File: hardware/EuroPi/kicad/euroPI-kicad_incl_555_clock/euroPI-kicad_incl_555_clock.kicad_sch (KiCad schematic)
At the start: 119 parts, among them J1 Output 1 Jack, J10 Eurorack Power 2x8 16p, J11 Conn_01x13_Socket, J12 OLED 64x128, J13 USB_B_Micro, J14 Conn_01x03_Pin, J15 Conn_01x04_Pin, J16 Conn_02x04_Top_Bottom, J17 Conn_01x13_Pin, J18 Conn_01x04_Pin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

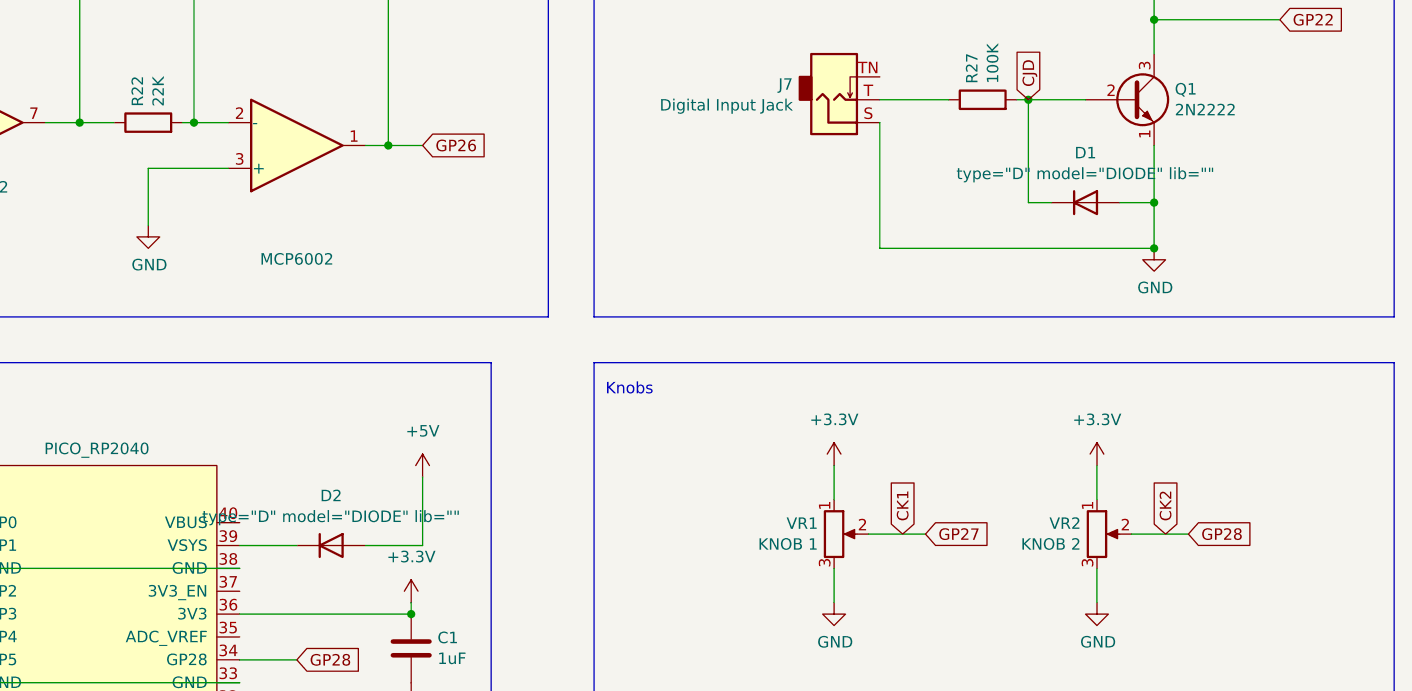
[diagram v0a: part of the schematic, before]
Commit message: wip tried a reroute should move power rail caps closer i think
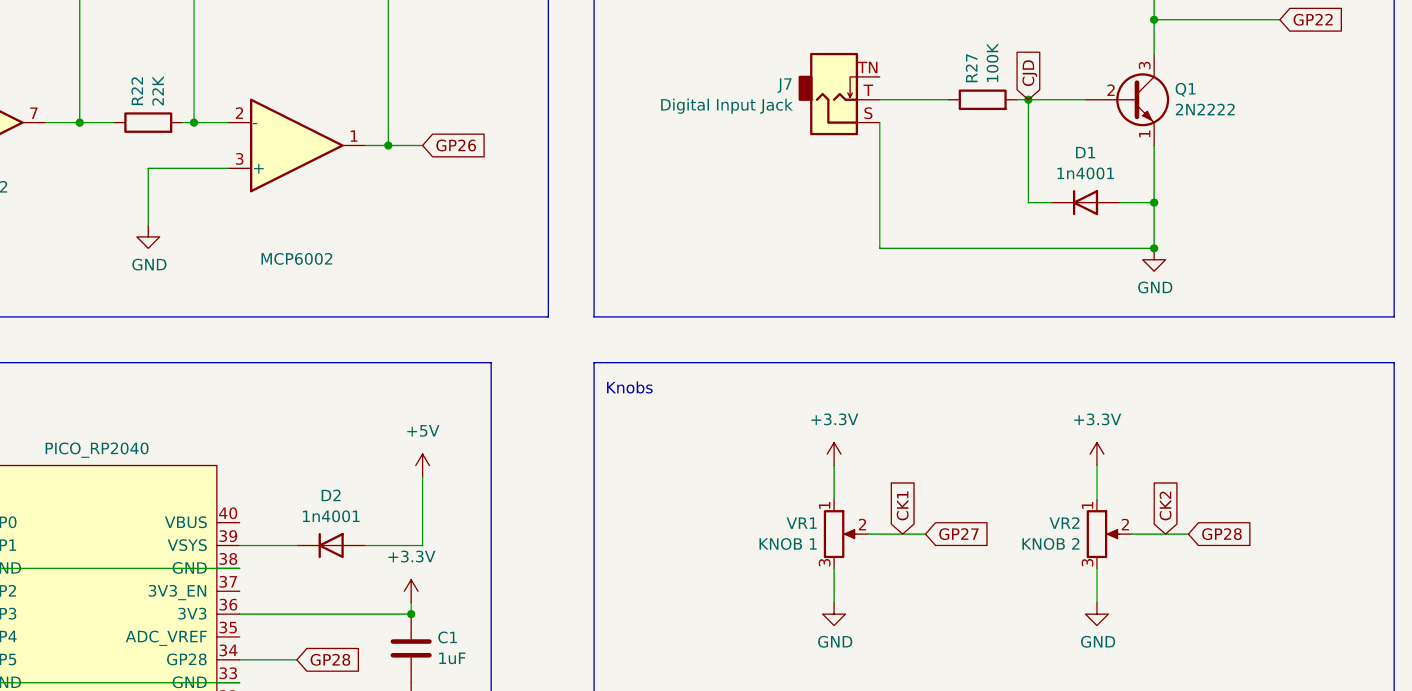
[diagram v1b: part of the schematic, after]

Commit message: reorg continued mainly trying to get power filtering better situated
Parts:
- O, O? (x8): footprint Package_DIP:DIP-14_W7.62mm_Socket -> Library:DIP-14_W7.62mm_Socket_gap_in_the_middle
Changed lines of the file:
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@@
       (effects (font (size 1.27 1.27)))
     )
-    (property "Footprint" "Package_DIP:DIP-14_W7.62mm_Socket" (at 342.9 35.56 0)
+    (property "Footprint" "Library:DIP-14_W7.62mm_Socket_gap_in_the_middle" (at 342.9 35.56 0)
       (effects (font (size 1.27 1.27)) hide)
     )
@@
       (effects (font (size 1.27 1.27)))
     )
-    (property "Footprint" "Package_DIP:DIP-14_W7.62mm_Socket" (at 153.67 35.56 0)
+    (property "Footprint" "Library:DIP-14_W7.62mm_Socket_gap_in_the_middle" (at 153.67 35.56 0)
       (effects (font (size 1.27 1.27)) hide)
     )
@@
       (effects (font (size 1.27 1.27)))
     )
-    (property "Footprint" "Package_DIP:DIP-14_W7.62mm_Socket" (at 247.65 35.56 0)
+    (property "Footprint" "Library:DIP-14_W7.62mm_Socket_gap_in_the_middle" (at 247.65 35.56 0)
       (effects (font (size 1.27 1.27)) hide)
     )
@@
       (effects (font (size 1.27 1.27)))
     )
-    (property "Footprint" "Package_DIP:DIP-14_W7.62mm_Socket" (at 342.9 91.44 0)
+    (property "Footprint" "Library:DIP-14_W7.62mm_Socket_gap_in_the_middle" (at 342.9 91.44 0)
       (effects (font (size 1.27 1.27)) hide)
     )
@@
       (effects (font (size 1.27 1.27)))
     )
-    (property "Footprint" "Package_DIP:DIP-14_W7.62mm_Socket" (at 153.67 91.44 0)
+    (property "Footprint" "Library:DIP-14_W7.62mm_Socket_gap_in_the_middle" (at 153.67 91.44 0)
       (effects (font (size 1.27 1.27)) hide)
     )
@@
       (effects (font (size 1.27 1.27)))
     )
-    (property "Footprint" "Package_DIP:DIP-14_W7.62mm_Socket" (at 247.65 91.44 0)
+    (property "Footprint" "Library:DIP-14_W7.62mm_Socket_gap_in_the_middle" (at 247.65 91.44 0)
       (effects (font (size 1.27 1.27)) hide)
     )
@@
       (effects (font (size 1.27 1.27)))
     )
-    (property "Footprint" "Package_DIP:DIP-14_W7.62mm_Socket" (at 240.03 180.34 0)
+    (property "Footprint" "Library:DIP-14_W7.62mm_Socket_gap_in_the_middle" (at 240.03 180.34 0)
       (effects (font (size 1.27 1.27)) hide)
     )
@@
       (effects (font (size 1.27 1.27)))
     )
-    (property "Footprint" "Package_DIP:DIP-14_W7.62mm_Socket" (at 146.05 231.14 0)
+    (property "Footprint" "Library:DIP-14_W7.62mm_Socket_gap_in_the_middle" (at 146.05 231.14 0)
       (effects (font (size 1.27 1.27)) hide)
     )
@@
       (effects (font (size 1.27 1.27)))
     )
-    (property "Footprint" "Package_DIP:DIP-14_W7.62mm_Socket" (at 166.37 231.14 0)
+    (property "Footprint" "Library:DIP-14_W7.62mm_Socket_gap_in_the_middle" (at 166.37 231.14 0)
       (effects (font (size 1.27 1.27)) hide)
     )

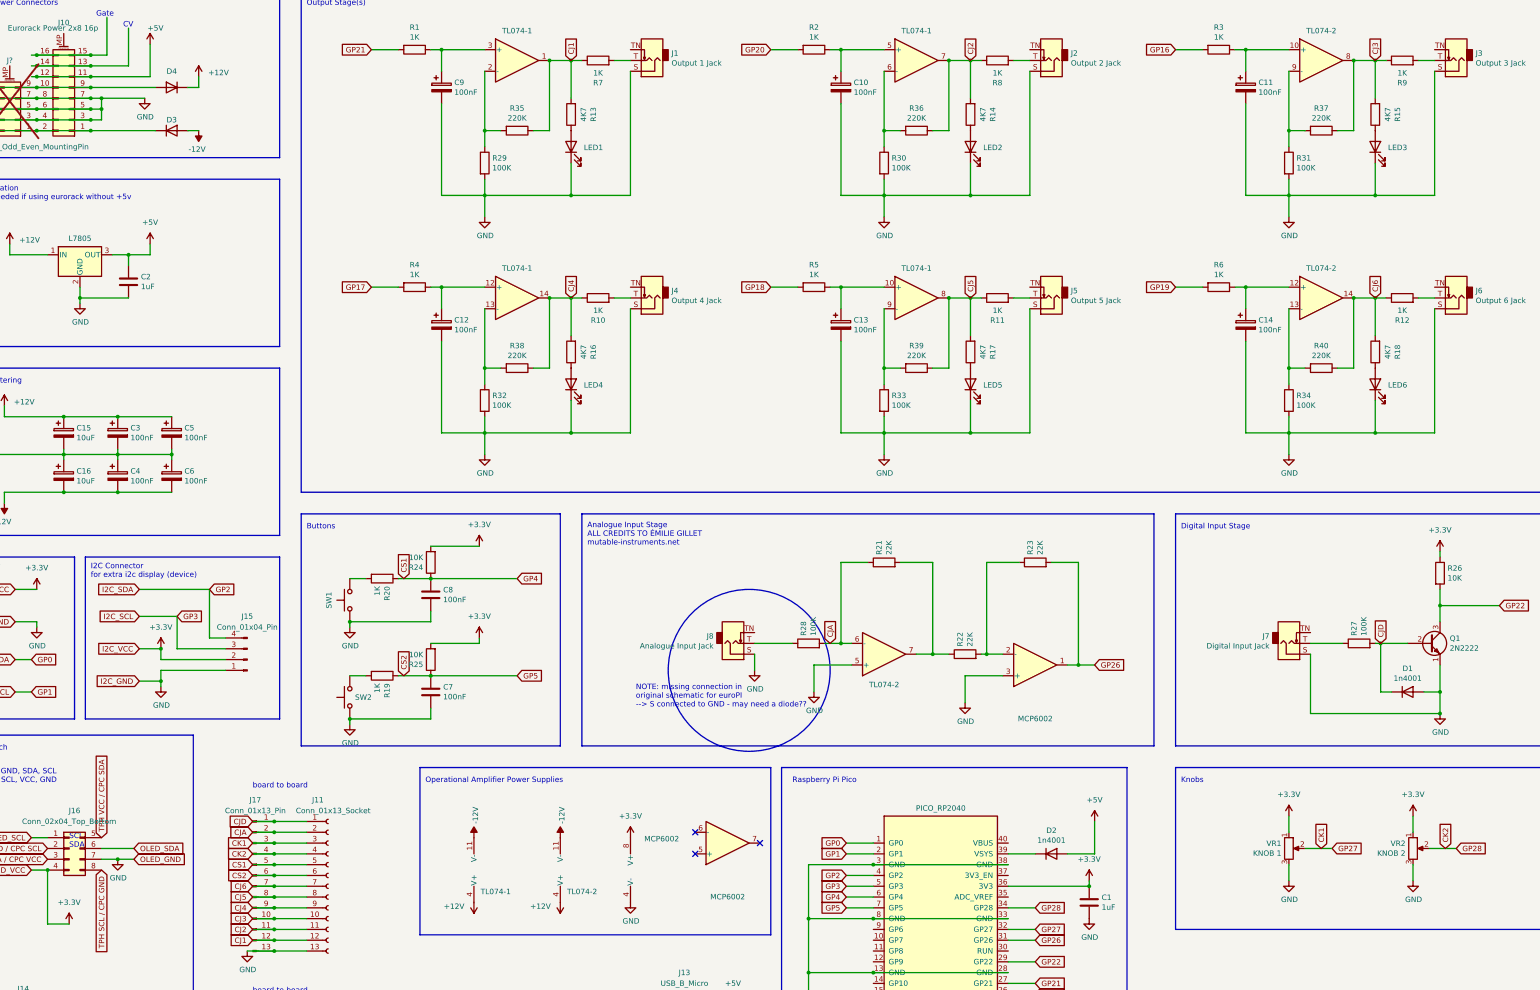
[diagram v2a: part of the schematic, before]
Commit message: updated with caps under sockets in order to improve power filtering as intended
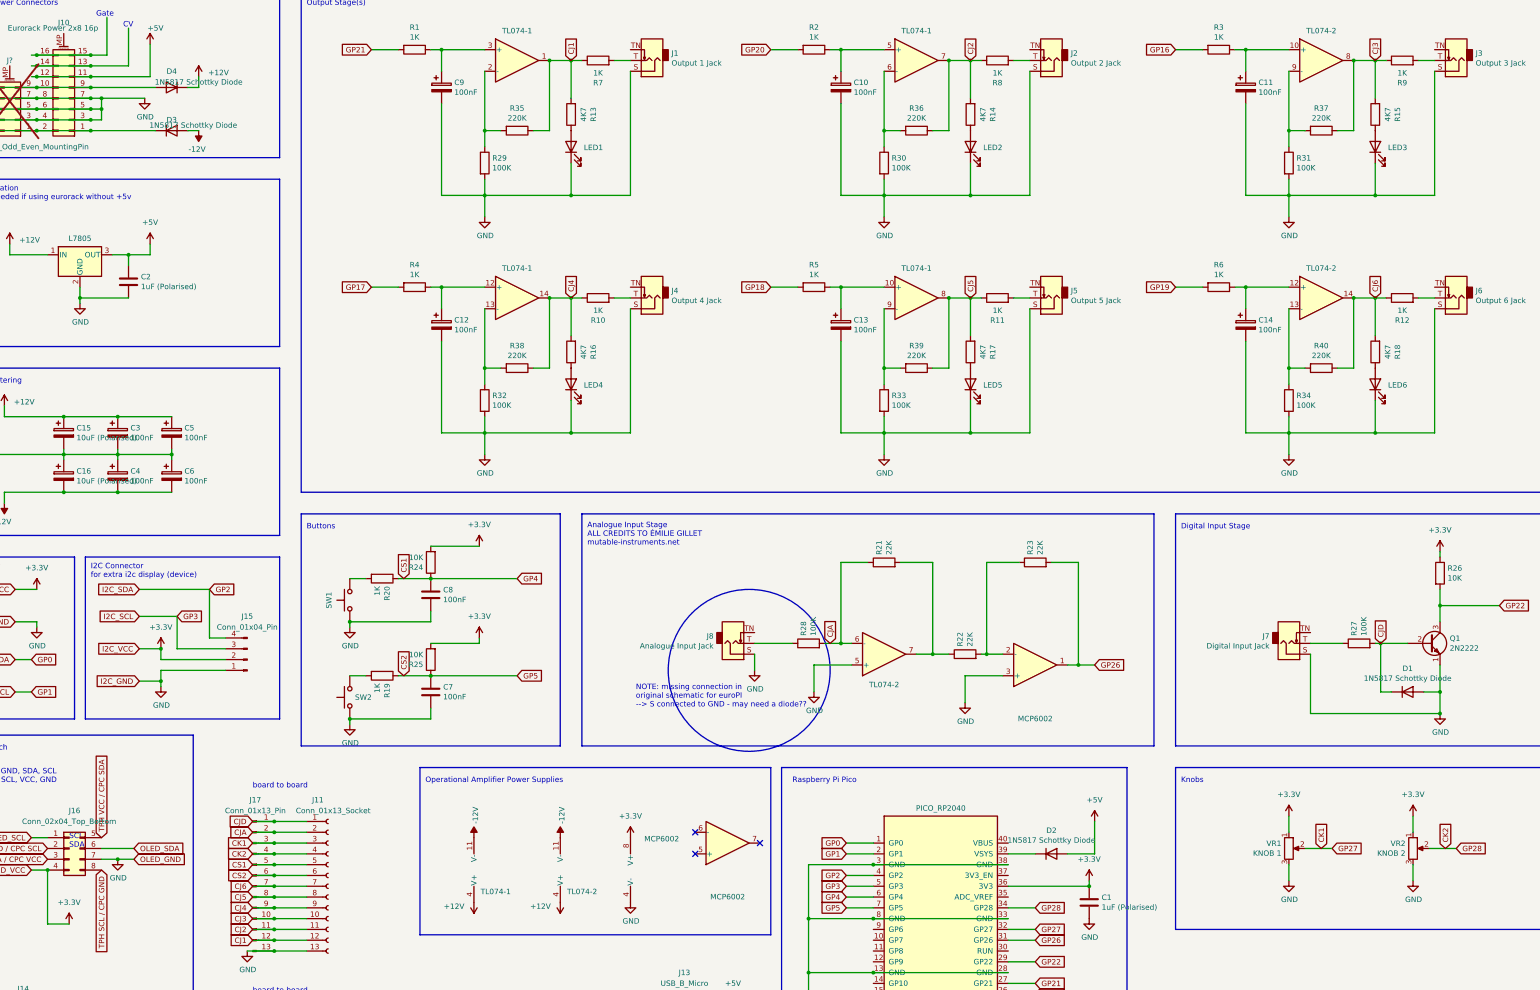
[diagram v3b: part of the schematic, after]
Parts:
- C1, C2: value 1uF -> 1uF (Polarised); footprint Capacitor_THT:C_Radial_D5.0mm_H11.0mm_P2.00mm -> Capacitor_THT:CP_Radial_D5.0mm_P2.00mm
- C15, C16: value 10uF -> 10uF (Polarised); footprint Capacitor_THT:C_Radial_D5.0mm_H11.0mm_P2.00mm -> Capacitor_THT:CP_Radial_D5.0mm_P2.00mm
- D1, D2, D3, D4: footprint Diode_THT:D_A-405_P2.54mm_Vertical_KathodeUp -> Diode_THT:D_DO-41_SOD81_P2.54mm_Vertical_KathodeUp
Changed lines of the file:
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@@
       (effects (font (size 1.27 1.27)) (justify left))
     )
-    (property "Value" "10uF" (at 51.2572 137.033 0)
+    (property "Value" "10uF (Polarised)" (at 51.2572 137.033 0)
       (effects (font (size 1.27 1.27)) (justify left))
     )
-    (property "Footprint" "Capacitor_THT:C_Radial_D5.0mm_H11.0mm_P2.00mm" (at 49.2252 139.7 0)
+    (property "Footprint" "Capacitor_THT:CP_Radial_D5.0mm_P2.00mm" (at 49.2252 139.7 0)
       (effects (font (size 1.27 1.27)) hide)
     )
@@
       (effects (font (size 1.27 1.27)))
     )
-    (property "Footprint" "Diode_THT:D_A-405_P2.54mm_Vertical_KathodeUp" (at 280.67 224.79 0)
+    (property "Footprint" "Diode_THT:D_DO-41_SOD81_P2.54mm_Vertical_KathodeUp" (at 280.67 224.79 0)
       (effects (font (size 1.27 1.27)) hide)
     )
@@
       (effects (font (size 1.27 1.27)) (justify left) hide)
     )
-    (property "Sim.Params" "1n4001" (at 191.77 5.08 0)
+    (property "Sim.Params" "1N5817 Schottky Diode" (at 191.77 5.08 0)
       (effects (font (size 0 0)) hide)
     )
@@
       (effects (font (size 1.27 1.27)))
     )
-    (property "Footprint" "Diode_THT:D_A-405_P2.54mm_Vertical_KathodeUp" (at 364.49 186.69 0)
+    (property "Footprint" "Diode_THT:D_DO-41_SOD81_P2.54mm_Vertical_KathodeUp" (at 364.49 186.69 0)
       (effects (font (size 1.27 1.27)) hide)
     )
@@
       (effects (font (size 1.27 1.27)) (justify left) hide)
     )
-    (property "Sim.Params" "1n4001" (at 0 0 0)
+    (property "Sim.Params" "1N5817 Schottky Diode" (at 0 0 0)
       (effects (font (size 0 0)) hide)
     )
@@
       (effects (font (size 1.27 1.27)) (justify left))
     )
-    (property "Value" "1uF" (at 66.421 91.313 0)
+    (property "Value" "1uF (Polarised)" (at 66.421 91.313 0)
       (effects (font (size 1.27 1.27)) (justify left))
     )
-    (property "Footprint" "Capacitor_THT:C_Radial_D5.0mm_H11.0mm_P2.00mm" (at 64.4652 93.98 0)
+    (property "Footprint" "Capacitor_THT:CP_Radial_D5.0mm_P2.00mm" (at 64.4652 93.98 0)
       (effects (font (size 1.27 1.27)) hide)
     )
@@
       (effects (font (size 1.27 1.27)) (justify left))
     )
-    (property "Value" "10uF" (at 51.2572 126.873 0)
+    (property "Value" "10uF (Polarised)" (at 51.2572 126.873 0)
       (effects (font (size 1.27 1.27)) (justify left))
     )
-    (property "Footprint" "Capacitor_THT:C_Radial_D5.0mm_H11.0mm_P2.00mm" (at 49.2252 129.54 0)
+    (property "Footprint" "Capacitor_THT:CP_Radial_D5.0mm_P2.00mm" (at 49.2252 129.54 0)
       (effects (font (size 1.27 1.27)) hide)
     )
@@
       (effects (font (size 1.27 1.27)))
     )
-    (property "Value" "${SIM.PARAMS}" (at 86.36 52.07 0)
-      (effects (font (size 1.27 1.27)) hide)
+    (property "Value" "${SIM.PARAMS}" (at 78.74 53.34 0)
+      (effects (font (size 1.27 1.27)))
     )
-    (property "Footprint" "Diode_THT:D_A-405_P2.54mm_Vertical_KathodeUp" (at 73.66 54.61 0)
+    (property "Footprint" "Diode_THT:D_DO-41_SOD81_P2.54mm_Vertical_KathodeUp" (at 73.66 54.61 0)
       (effects (font (size 1.27 1.27)) hide)
     )
@@
       (effects (font (size 1.27 1.27)) (justify left) hide)
     )
-    (property "Sim.Params" "1n4001" (at 3.81 7.62 0)
+    (property "Sim.Params" "1N5817 Schottky Diode" (at 3.81 7.62 0)
       (effects (font (size 0 0)) hide)
     )
@@
     )
     (property "Value" "${SIM.PARAMS}" (at 80.01 43.18 0)
-      (effects (font (size 1.27 1.27)) hide)
+      (effects (font (size 1.27 1.27)))
     )
-    (property "Footprint" "Diode_THT:D_A-405_P2.54mm_Vertical_KathodeUp" (at 73.66 44.45 0)
+    (property "Footprint" "Diode_THT:D_DO-41_SOD81_P2.54mm_Vertical_KathodeUp" (at 73.66 44.45 0)
       (effects (font (size 1.27 1.27)) hide)
     )
@@
       (effects (font (size 1.27 1.27)) (justify left) hide)
     )
-    (property "Sim.Params" "1n4001" (at 3.81 7.62 0)
+    (property "Sim.Params" "1N5817 Schottky Diode" (at 3.81 7.62 0)
       (effects (font (size 0 0)) hide)
     )
@@
       (effects (font (size 1.27 1.27)) (justify left))
     )
-    (property "Value" "1uF" (at 292.481 237.363 0)
+    (property "Value" "1uF (Polarised)" (at 292.481 237.363 0)
       (effects (font (size 1.27 1.27)) (justify left))
     )
-    (property "Footprint" "Capacitor_THT:C_Radial_D5.0mm_H11.0mm_P2.00mm" (at 290.5252 240.03 0)
+    (property "Footprint" "Capacitor_THT:CP_Radial_D5.0mm_P2.00mm" (at 290.5252 240.03 0)
       (effects (font (size 1.27 1.27)) hide)
     )

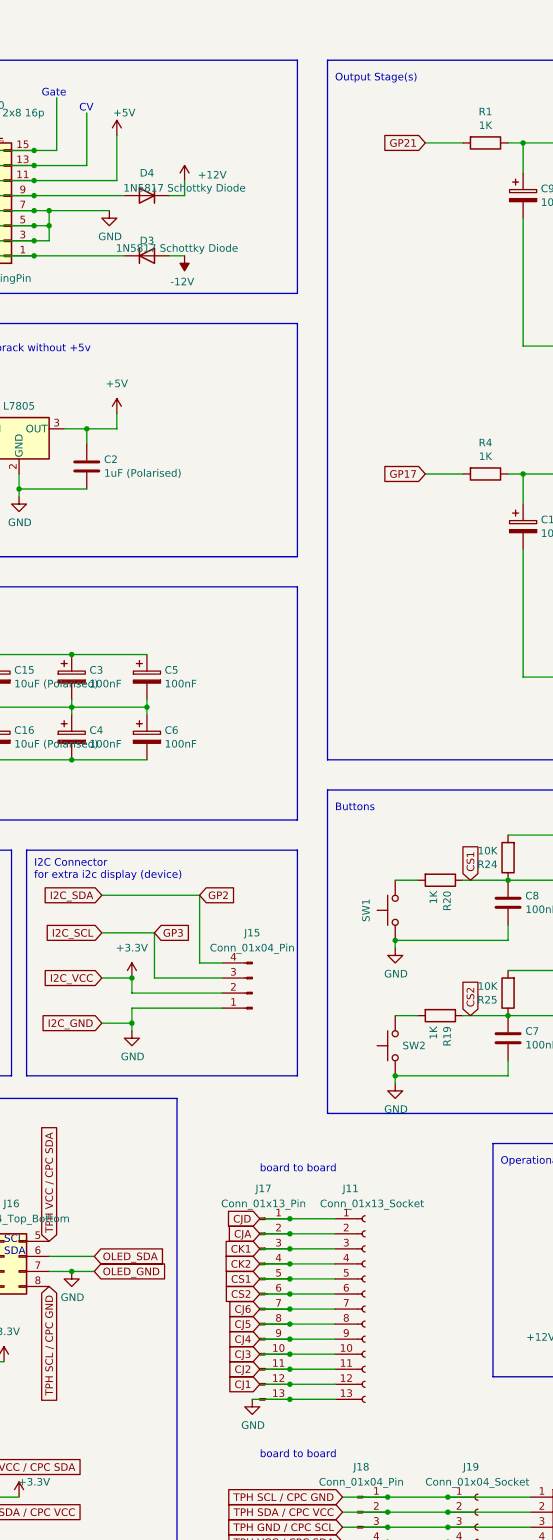
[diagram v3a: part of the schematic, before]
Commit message: incl standoffs to GND removed GND pin on headers
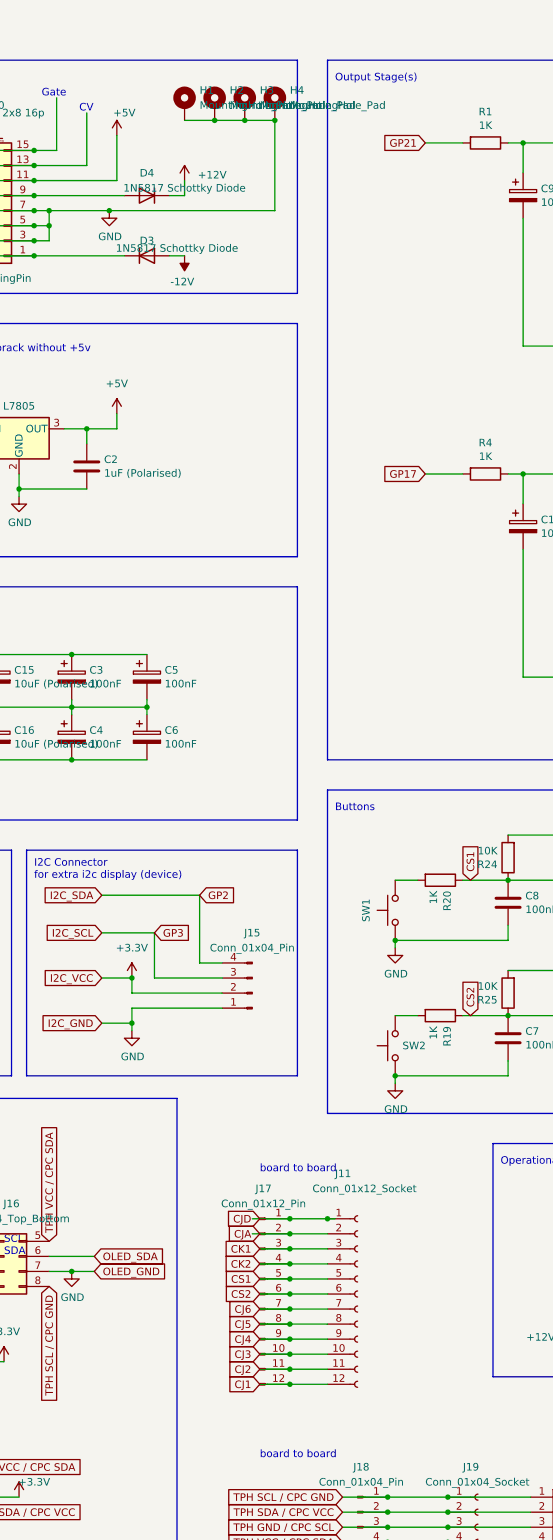
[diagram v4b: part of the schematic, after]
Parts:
- added H1, H2, H3, H4: MountingHole_Pad, MountingHole:MountingHole_2.7mm_M2.5_ISO14580_Pad_TopBottom, symbol Mechanical:MountingHole_Pad
- D1, D2, D3, D4: value ${SIM.PARAMS} -> 1N5817 Schottky Diode
- J11: value Conn_01x13_Socket -> Conn_01x12_Socket; footprint Connector_PinSocket_2.54mm:PinSocket_1x13_P2.54mm_Vertical -> Connector_PinSocket_2.54mm:PinSocket_1x12_P2.54mm_Vertical; symbol Connector:Conn_01x13_Socket -> Connector:Conn_01x12_Socket
- J17: value Conn_01x13_Pin -> Conn_01x12_Pin; footprint Connector_PinSocket_2.54mm:PinSocket_1x13_P2.54mm_Vertical -> Connector_PinHeader_2.54mm:PinHeader_1x12_P2.54mm_Vertical; symbol Connector:Conn_01x13_Pin -> Connector:Conn_01x12_Pin
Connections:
- net GND: now also H1.1, H2.1, H3.1, H4.1; no longer J11.13 (Pin_13), J17.13 (Pin_13)
